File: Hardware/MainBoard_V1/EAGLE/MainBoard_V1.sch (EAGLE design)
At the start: 25 parts, among them IC1 REG1117, J1 NANO_FOOTPRINTNANO, J4 I2C, K1 RELAY-SPDT-JZC-11F, Q2 600mA/40V, Q3 600mA/40V, U1 MOC3021M, U2 TXB0104, U4 MCT2EM, X2 AC

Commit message: SubBoard_V1 initial state
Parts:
- removed U2: TXB0104, SparkFun-IC-Comms:TXB0104PWRSOIC14
- added JP1: JUMPER-SMT_2_NO_SILK, SparkFun-Jumpers:JUMPER-SMT_2_NO_SILK
- added U$1, U$2, U$3, U$4, U$5, U$6, U$7, U$8: FIDUCIAL, adafruit:FIDUCIAL
- added U3: (no value), adafruit:TXS0102
- D2: value 1A/50V/1.1V -> S1M; device SparkFun-DiscreteSemi:DIODE-PTH -> diode:S1M
- R1, R3, R4, R5, R6: device rcl:R-US_R0402 -> rcl:R-US_R0603
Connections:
- net 3V3: now also U3.OE, U3.VCCA; no longer U2.OE, U2.VCCA
- net 5V: now also JP1.2, U3.VCCB; no longer U2.VCCB
- net A4: now also U3.B2; no longer U2.B3
- net A5: now also U3.B1; no longer U2.B4
- net GND: now also U3.GND; no longer U2.GND
- net SCL: now also U3.A1; no longer U2.A4
- net SDA: now also U3.A2; no longer U2.A3
- net VIN: now also JP1.1
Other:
- moved on the sheet: J2, J3

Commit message: Mounting holes
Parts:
- added C2: 220uF, rcl:CPOL-USE2.5-6
- added C3: (no value), rcl:C-US150-064X183
- added L1: DFKH14, inductors:DFKH14
- added PSU2: HLK-10M05, discrete:HLK-10M05
- added R8: VARISTOR-7,5, varistor:VARISTOR-7,5
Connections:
- removed net ACNEG: K1.MAIN, PSU1.AC_N, R7.1, TR1.A1, U4.C, X2-2.1, X2-2.2
- removed net ACPOS: PSU1.AC_L, R2.2, X2-1.1, X2-1.2
- new net ACL: C3.1, K1.MAIN, L1.1, PSU1.AC_L, R2.2, R7.1, R8.1, TR1.A1, X2-2.1, X2-2.2
- new net ACN: C3.2, D1.A, L1.3, PSU1.AC_N, R8.2, X2-1.1, X2-1.2
- new net N$12: L1.4, PSU2.AC_N
- new net N$7: L1.2, PSU2.AC_L
- net GND: now also C2.-, PSU2.VO-
- net N$5: now also U4.C; no longer D1.A
- net VIN: now also C2.+, PSU2.VO+
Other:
- moved on the sheet: IC1, J4, JP1, PSU1, R2, U3

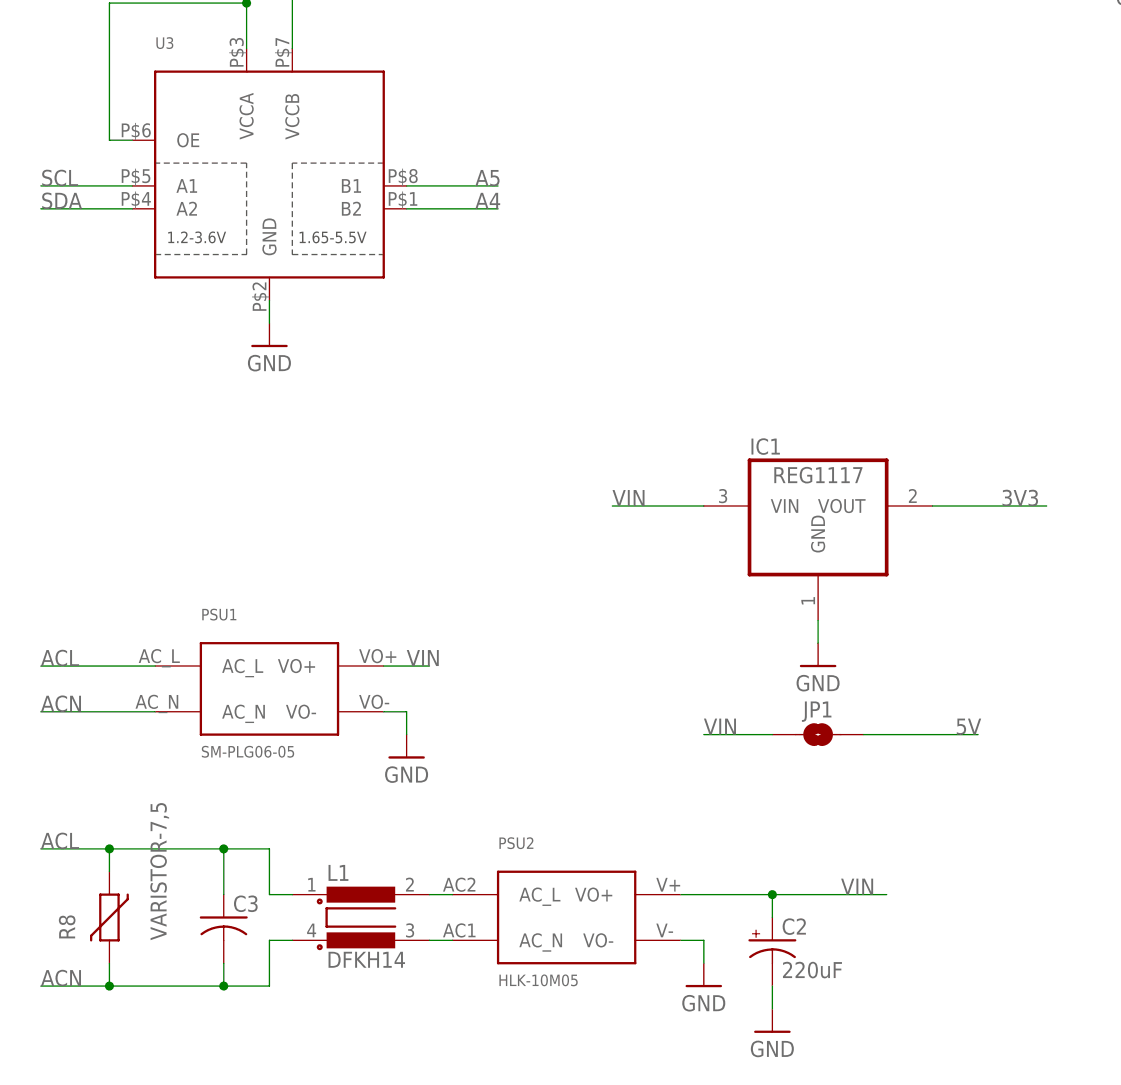
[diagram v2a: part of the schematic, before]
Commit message: All SMD to the top layer
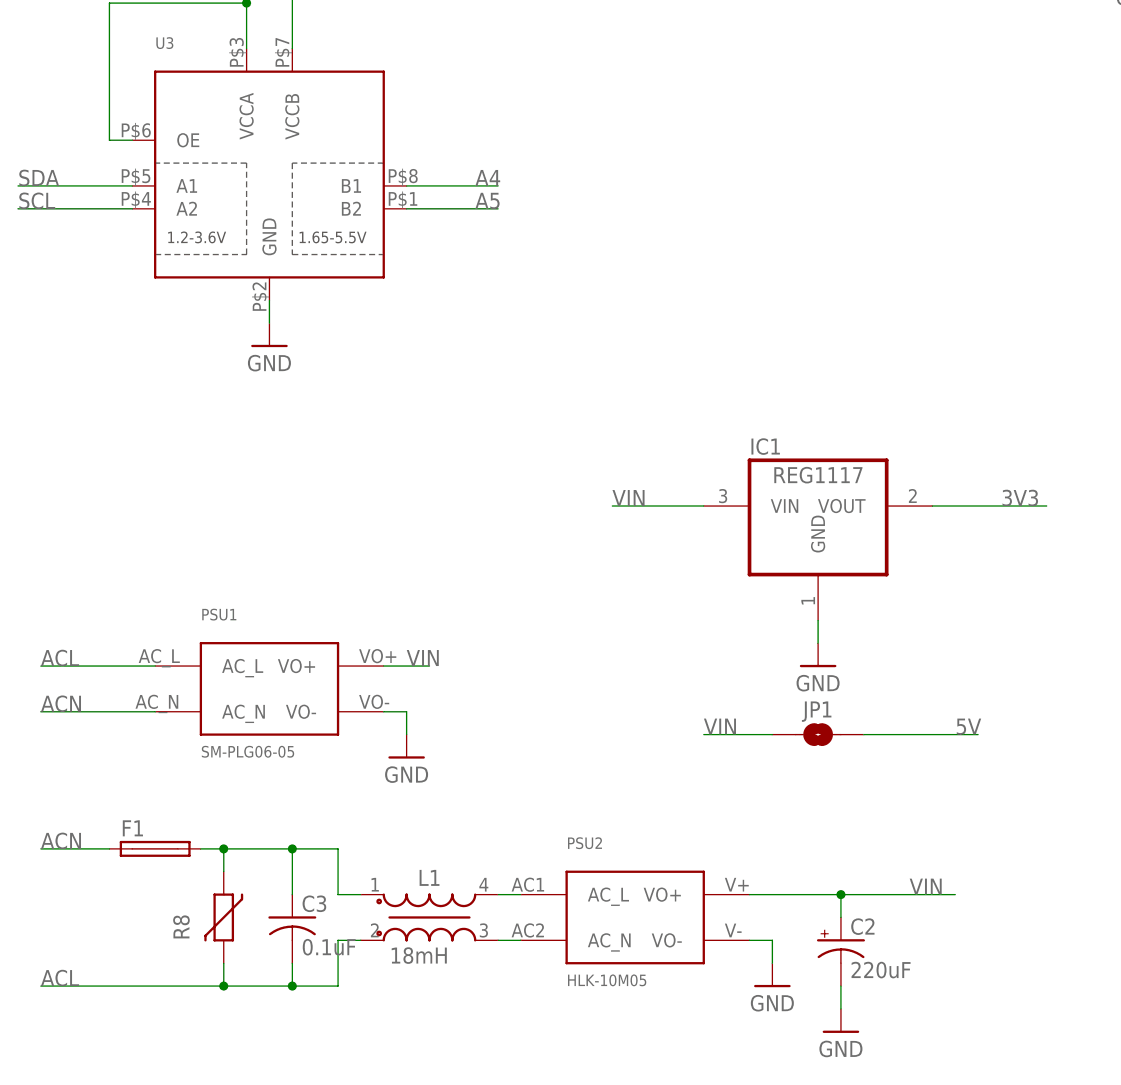
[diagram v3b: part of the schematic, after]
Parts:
- added F1: FUSETE5, fuse:FUSETE5
- C3: value (none) -> 0.1uF; device rcl:C-US150-064X183 -> rcl:C-US150-054X183
- L1: value DFKH14 -> 18mH; device inductors:DFKH14 -> Wurth_EMC Components_WE-TFC:WE-TFC_UU9.8V_744862180
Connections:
- new net ACN1: C3.1, F1.2, L1.1, R8.1
- net A4: now also U3.B1; no longer U3.B2
- net A5: now also U3.B2; no longer U3.B1
- net ACL: now also C3.2, L1.2, R8.2; no longer C3.1, L1.1, R8.1
- net ACN: now also F1.1; no longer C3.2, L1.3, R8.2
- net N$12: now also L1.3; no longer L1.4
- net N$7: now also L1.4; no longer L1.2
- net SCL: now also U3.A2; no longer U3.A1
- net SDA: now also U3.A1; no longer U3.A2
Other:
- moved on the sheet: C2, C3, PSU2, R8

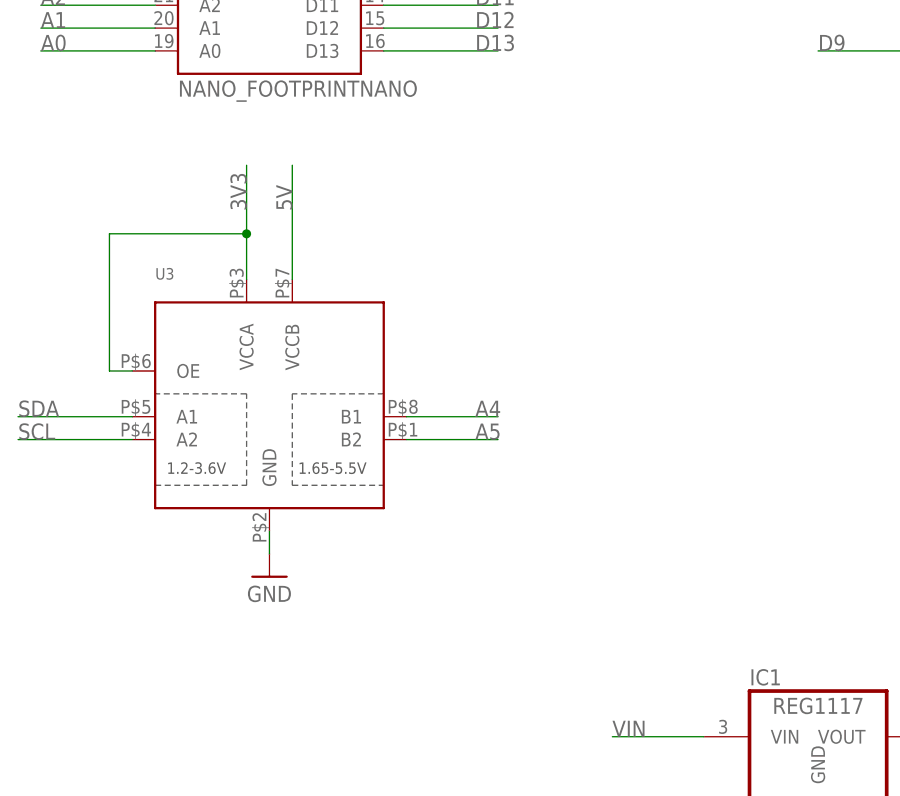
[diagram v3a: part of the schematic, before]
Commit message: I2C pullups
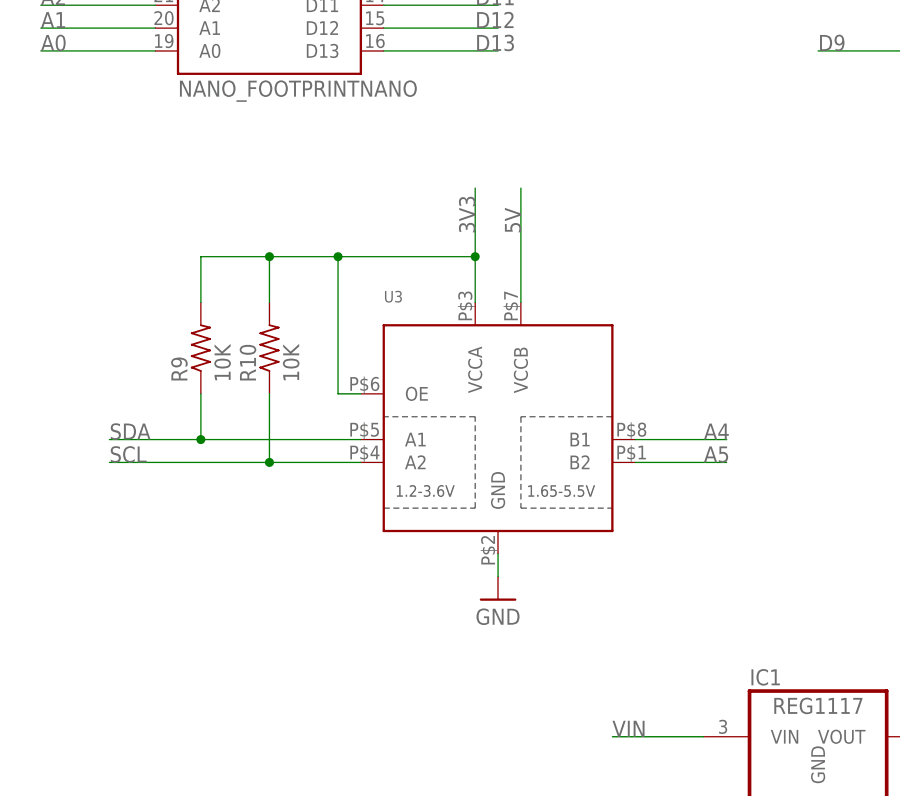
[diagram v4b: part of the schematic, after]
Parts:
- added R10, R9: 10K, rcl:R-US_R0603
- C1: LCSC (none) -> C2893639
- D1, D2: LCSC (none) -> C155378
- IC1: LCSC (none) -> C26537
- J2, J3: LCSC (none) -> C2894938
- J4: LCSC (none) -> C160390
- K1: LCSC (none) -> C74541
- Q2, Q3: LCSC (none) -> C82460
- R1, R3: LCSC (none) -> C23179
- R2: LCSC (none) -> C22961
- R4, R5, R6: LCSC (none) -> C98220
- R7: LCSC (none) -> C38808
- TR1: LCSC (none) -> C145130
- U1: LCSC (none) -> C123202
- U3: LCSC (none) -> C2677417
- U4: LCSC (none) -> C258259
- X1, X2: LCSC (none) -> C305817
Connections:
- net 3V3: now also R10.2, R9.2
- net SCL: now also R10.1
- net SDA: now also R9.1
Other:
- moved on the sheet: U3

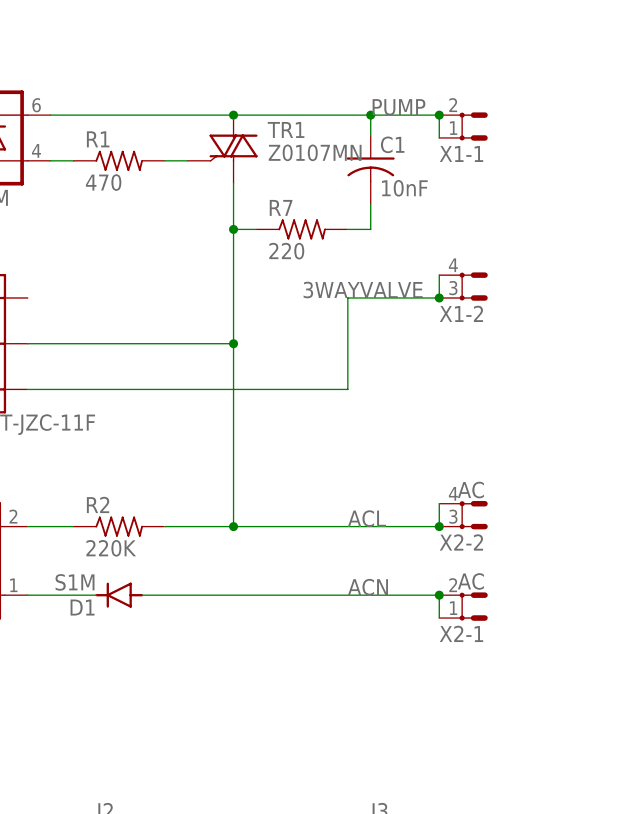
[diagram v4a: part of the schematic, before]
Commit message: Spade connectors BOM fix
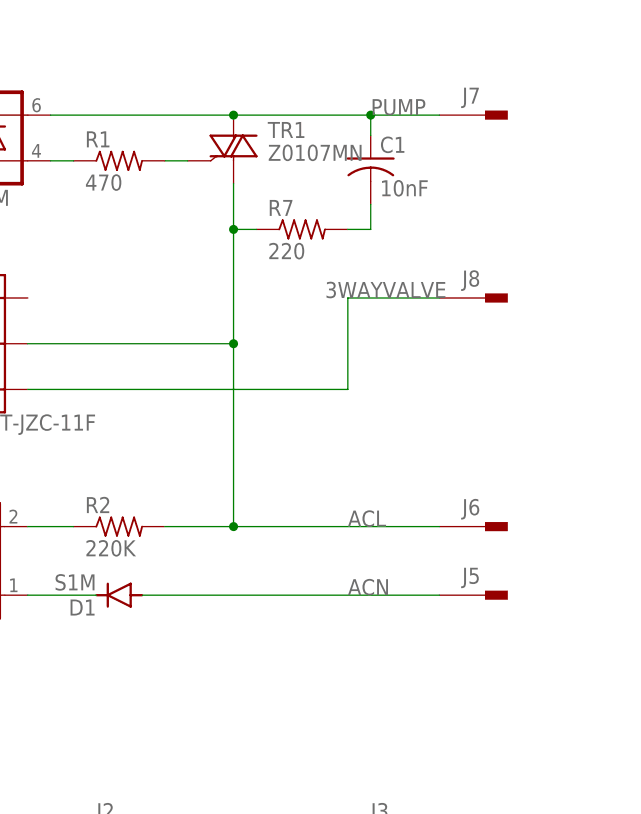
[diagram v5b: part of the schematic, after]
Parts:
- removed X1: (no value), con-rib:SH5-2
- removed X2: AC, con-rib:SH5-2
- added J5, J6, J7, J8: PIN262409-1, con-faston:PIN262409-1
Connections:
- net 3WAYVALVE: now also J8.1; no longer X1-2.1, X1-2.2
- net ACL: now also J6.1; no longer X2-2.1, X2-2.2
- net ACN: now also J5.1; no longer X2-1.1, X2-1.2
- net PUMP: now also J7.1; no longer X1-1.1, X1-1.2
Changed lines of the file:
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@@
 <attribute name="LCSC" value="C123202"/>
-</part>
-<part name="X2" library="con-rib" library_urn="urn:adsk.eagle:library:183" deviceset="SH5-2" device="" package3d_urn="urn:adsk.eagle:package:9989/1" value="AC">
-<attribute name="LCSC" value="C305817"/>
-</part>
-<part name="X1" library="con-rib" library_urn="urn:adsk.eagle:library:183" deviceset="SH5-2" device="" package3d_urn="urn:adsk.eagle:package:9989/1">
-<attribute name="LCSC" value="C305817"/>
 </part>
 <part name="J1" library="SparkFun-Boards" deviceset="NANO_FOOTPRINT" device="NANO"/>
@@
 <attribute name="LCSC" value="C98220"/>
 </part>
+<part name="J5" library="con-faston" library_urn="urn:adsk.eagle:library:144" deviceset="PIN2" device="62409-1" package3d_urn="urn:adsk.eagle:package:6760/1" value="">
+<attribute name="LCSC" value="C305817"/>
+</part>
+<part name="J6" library="con-faston" library_urn="urn:adsk.eagle:library:144" deviceset="PIN2" device="62409-1" package3d_urn="urn:adsk.eagle:package:6760/1" value="">
+<attribute name="LCSC" value="C305817"/>
+</part>
+<part name="J7" library="con-faston" library_urn="urn:adsk.eagle:library:144" deviceset="PIN2" device="62409-1" package3d_urn="urn:adsk.eagle:package:6760/1" value="">
+<attribute name="LCSC" value="C305817"/>
+</part>
+<part name="J8" library="con-faston" library_urn="urn:adsk.eagle:library:144" deviceset="PIN2" device="62409-1" package3d_urn="urn:adsk.eagle:package:6760/1" value="">
+<attribute name="LCSC" value="C305817"/>
+</part>
 </parts>
 <sheets>
@@
 <attribute name="VALUE" x="165.7096" y="160.0962" size="1.778" layer="96"/>
 <attribute name="LCSC" x="172.72" y="167.64" size="1.778" layer="96" display="off"/>
-</instance>
-<instance part="X2" gate="-1" x="231.14" y="116.84" smashed="yes" rot="R180">
-<attribute name="NAME" x="231.14" y="113.411" size="1.778" layer="95" rot="R180"/>
-<attribute name="VALUE" x="231.14" y="119.253" size="1.778" layer="96" rot="R180"/>
-</instance>
-<instance part="X2" gate="-2" x="231.14" y="127" smashed="yes" rot="R180">
-<attribute name="NAME" x="231.14" y="123.571" size="1.778" layer="95" rot="R180"/>
-<attribute name="VALUE" x="231.14" y="129.413" size="1.778" layer="96" rot="R180"/>
-<attribute name="LCSC" x="231.14" y="127" size="1.778" layer="96" rot="R180" display="off"/>
-</instance>
-<instance part="X1" gate="-1" x="231.14" y="170.18" smashed="yes" rot="R180">
-<attribute name="NAME" x="231.14" y="166.751" size="1.778" layer="95" rot="R180"/>
-<attribute name="VALUE" x="231.14" y="172.593" size="1.778" layer="96" rot="R180"/>
-<attribute name="LCSC" x="231.14" y="170.18" size="1.778" layer="96" rot="R180" display="off"/>
-</instance>
-<instance part="X1" gate="-2" x="231.14" y="152.4" smashed="yes" rot="R180">
-<attribute name="NAME" x="231.14" y="148.971" size="1.778" layer="95" rot="R180"/>
-<attribute name="VALUE" x="231.14" y="154.813" size="1.778" layer="96" rot="R180"/>
 </instance>
 <instance part="J1" gate="G$1" x="35.56" y="154.94" smashed="yes">
@@
 <attribute name="LCSC" x="35.56" y="106.68" size="1.778" layer="96" rot="R90" display="off"/>
 </instance>
+<instance part="J5" gate="-1" x="231.14" y="116.84" smashed="yes">
+<attribute name="NAME" x="228.6" y="118.11" size="1.778" layer="95"/>
+<attribute name="VALUE" x="228.6" y="114.3" size="1.778" layer="96"/>
+<attribute name="LCSC" x="231.14" y="116.84" size="1.778" layer="96" display="off"/>
+</instance>
+<instance part="J6" gate="-1" x="231.14" y="124.46" smashed="yes">
+<attribute name="NAME" x="228.6" y="125.73" size="1.778" layer="95"/>
+<attribute name="VALUE" x="228.6" y="121.92" size="1.778" layer="96"/>
+<attribute name="LCSC" x="231.14" y="124.46" size="1.778" layer="96" display="off"/>
+</instance>
+<instance part="J7" gate="-1" x="231.14" y="170.18" smashed="yes">
+<attribute name="NAME" x="228.6" y="171.45" size="1.778" layer="95"/>
+<attribute name="VALUE" x="228.6" y="167.64" size="1.778" layer="96"/>
+<attribute name="LCSC" x="231.14" y="170.18" size="1.778" layer="96" display="off"/>
+</instance>
+<instance part="J8" gate="-1" x="231.14" y="149.86" smashed="yes">
+<attribute name="NAME" x="228.6" y="151.13" size="1.778" layer="95"/>
+<attribute name="VALUE" x="228.6" y="147.32" size="1.778" layer="96"/>
+<attribute name="LCSC" x="231.14" y="149.86" size="1.778" layer="96" display="off"/>
+</instance>
 </instances>
 <busses>
@@
 <pinref part="U1" gate="G$1" pin="A2"/>
 <pinref part="TR1" gate="G$1" pin="A2"/>
-<pinref part="X1" gate="-1" pin="1"/>
-<pinref part="X1" gate="-1" pin="2"/>
-<wire x1="226.06" y1="170.18" x2="226.06" y2="167.64" width="0.1524" layer="91"/>
 <wire x1="203.2" y1="170.18" x2="218.44" y2="170.18" width="0.1524" layer="91"/>
 <junction x="203.2" y="170.18"/>
-<junction x="226.06" y="170.18"/>
 <label x="218.44" y="170.18" size="1.778" layer="95"/>
 <pinref part="C1" gate="G$1" pin="1"/>
@@
 <wire x1="218.44" y1="167.894" x2="218.44" y2="170.18" width="0.1524" layer="91"/>
 <junction x="218.44" y="170.18"/>
+<pinref part="J7" gate="-1" pin="1"/>
 </segment>
 </net>
 <net name="ACN" class="0">
 <segment>
-<pinref part="X2" gate="-1" pin="2"/>
-<pinref part="X2" gate="-1" pin="1"/>
-<wire x1="226.06" y1="116.84" x2="226.06" y2="114.3" width="0.1524" layer="91"/>
 <label x="215.9" y="116.84" size="1.778" layer="95"/>
 <pinref part="D1" gate="G$1" pin="A"/>
 <wire x1="193.04" y1="116.84" x2="226.06" y2="116.84" width="0.1524" layer="91"/>
-<junction x="226.06" y="116.84"/>
+<pinref part="J5" gate="-1" pin="1"/>
 </segment>
 <segment>
@@
 <net name="3WAYVALVE" class="0">
 <segment>
-<pinref part="X1" gate="-2" pin="2"/>
-<pinref part="X1" gate="-2" pin="1"/>
-<wire x1="226.06" y1="149.86" x2="226.06" y2="152.4" width="0.1524" layer="91"/>
 <pinref part="K1" gate="K$1" pin="NO"/>
 <wire x1="180.34" y1="139.7" x2="215.9" y2="139.7" width="0.1524" layer="91"/>
 <wire x1="226.06" y1="149.86" x2="215.9" y2="149.86" width="0.1524" layer="91"/>
 <wire x1="215.9" y1="149.86" x2="215.9" y2="139.7" width="0.1524" layer="91"/>
-<junction x="226.06" y="149.86"/>
-<label x="210.82" y="149.86" size="1.778" layer="95"/>
+<label x="213.36" y="149.86" size="1.778" layer="95"/>
+<pinref part="J8" gate="-1" pin="1"/>
 </segment>
 </net>
@@
 <net name="ACL" class="0">
 <segment>
-<pinref part="X2" gate="-2" pin="1"/>
 <wire x1="203.2" y1="162.56" x2="203.2" y2="157.48" width="0.1524" layer="91"/>
 <wire x1="203.2" y1="157.48" x2="203.2" y2="144.78" width="0.1524" layer="91"/>
@@
 <pinref part="TR1" gate="G$1" pin="A1"/>
 <label x="215.9" y="124.46" size="1.778" layer="95"/>
-<pinref part="X2" gate="-2" pin="2"/>
-<wire x1="226.06" y1="127" x2="226.06" y2="124.46" width="0.1524" layer="91"/>
-<junction x="226.06" y="124.46"/>
 <pinref part="R7" gate="G$1" pin="1"/>
 <wire x1="205.74" y1="157.48" x2="203.2" y2="157.48" width="0.1524" layer="91"/>
@@
 <wire x1="195.58" y1="124.46" x2="203.2" y2="124.46" width="0.1524" layer="91"/>
 <junction x="203.2" y="124.46"/>
-</segment>
-<segment>
+<pinref part="J6" gate="-1" pin="1"/>
+</segment>
+<segment>
